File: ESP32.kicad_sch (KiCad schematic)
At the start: 1 part

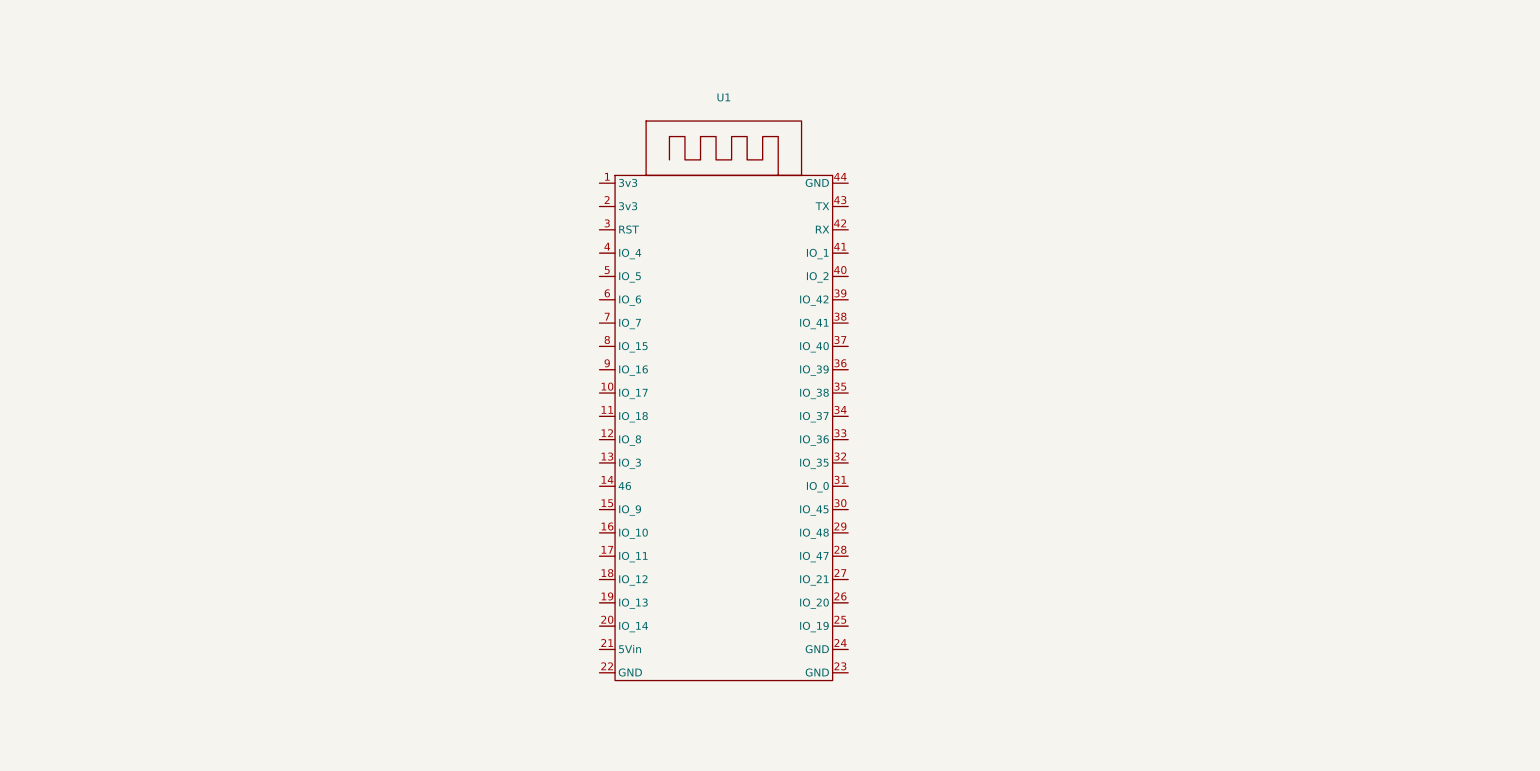
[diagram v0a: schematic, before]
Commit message: added all block interface pins
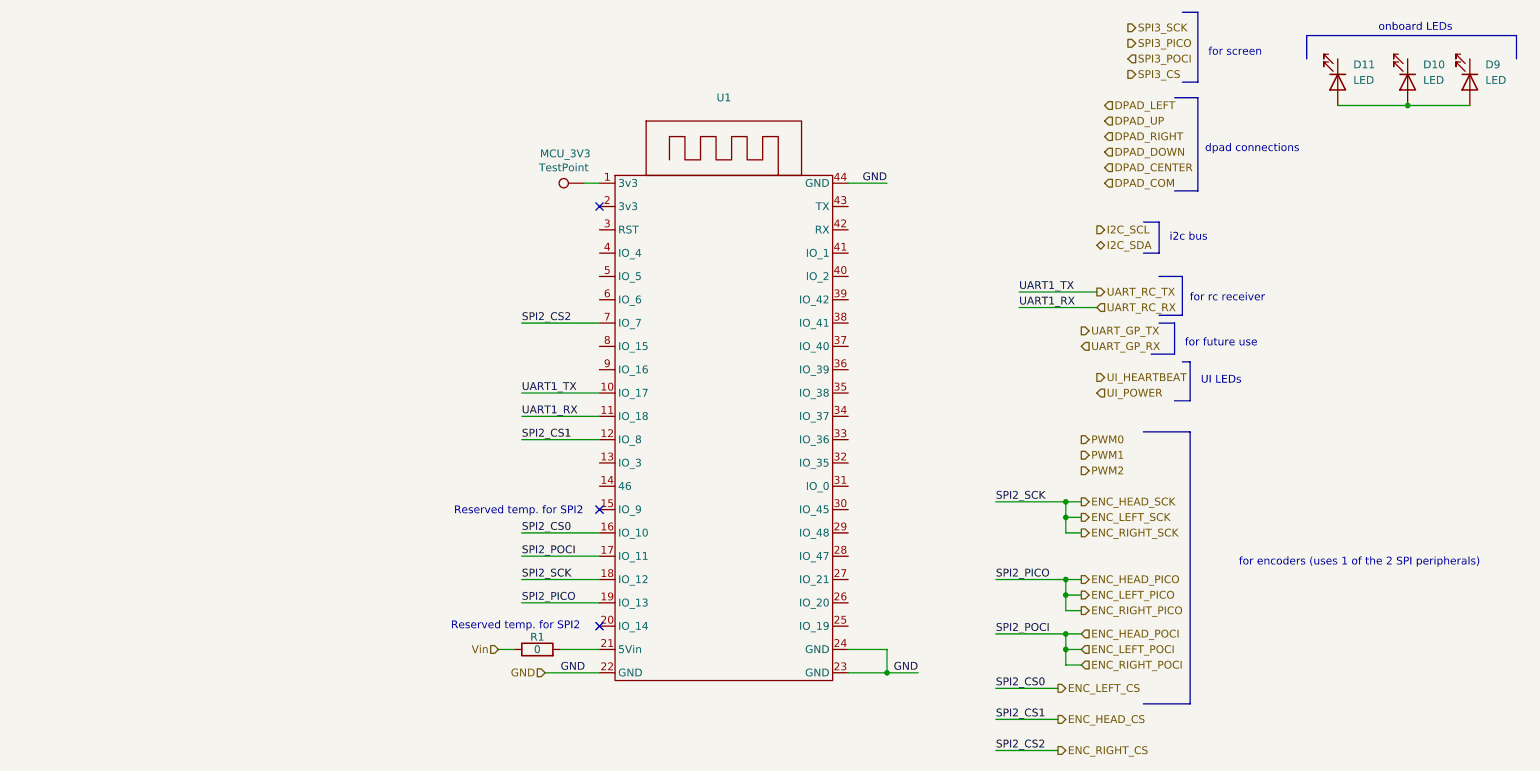
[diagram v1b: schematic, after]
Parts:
- added D10, D11, D9: LED, symbol Device:LED
- added MCU_3V3: TestPoint, symbol Connector:TestPoint
- added R1: 0, symbol Device:R
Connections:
- net at U1.1 (3v3): now also MCU_3V3.1
- net UART_RC_TX: now reaches U1.10 (IO_17)
- net UART_RC_RX: now reaches U1.11 (IO_18)
- net ENC_HEAD_CS: now reaches U1.12 (IO_8)
- net ENC_LEFT_CS: now reaches U1.16 (IO_10)
- net ENC_HEAD_POCI: now reaches U1.17 (IO_11)
- net ENC_HEAD_SCK: now reaches U1.18 (IO_12)
- net ENC_HEAD_PICO: now reaches U1.19 (IO_13)
- net at U1.21 (5Vin): now also R1.2
- net GND: now reaches U1.22 (GND)
- net GND: now also U1.23 (GND), U1.24 (GND), U1.44 (GND)
- net ENC_RIGHT_CS: now reaches U1.7 (IO_7)
- new net: D10.2 (A), D11.2 (A), D9.2 (A)
- new net Vin: R1.1
- no-connect marks 0 -> 3
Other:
- note added: "Reserved temp. for SPI2"
- note added: "UI LEDs"
- note added: "dpad connections"
- note added: "for encoders (uses 1 of the 2 SPI peripherals)"
- note added: "for future use"
- note added: "for rc receiver"
- note added: "for screen"
- note added: "i2c bus"
- note added: "onboard LEDs"

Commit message: ESP32 mostly done
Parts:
- removed D10, D11, D9: LED, symbol Device:LED
- added Q1, Q2: BSS138, Package_TO_SOT_SMD:SOT-23, symbol Transistor_FET:BSS138
- added R2, R3, R4, R5, R6, R7: R, symbol Device:R
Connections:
- net GND is gone; now on net DPAD_COM: U1.22 (GND), U1.23 (GND), U1.24 (GND), U1.44 (GND)
- net DPAD_CENTER: now also U1.4 (IO_4)
- net DPAD_DOWN: now also U1.13 (IO_3)
- net DPAD_LEFT: now also U1.31 (IO_0)
- net DPAD_RIGHT: now also U1.41 (IO_1)
- net DPAD_UP: now also U1.40 (IO_2)
- net ENC_HEAD_CS: now also U1.5 (IO_5); no longer U1.12 (IO_8)
- net ENC_LEFT_CS: now also U1.6 (IO_6); no longer U1.16 (IO_10)
- net I2C_SCL: now also U1.9 (IO_16), R2.2
- net I2C_SDA: now also U1.8 (IO_15), R3.2
- net UART_GP_RX: now also U1.28 (IO_47)
- net UART_GP_TX: now also U1.29 (IO_48)
- net UART_RC_RX: no longer U1.11 (IO_18)
- net UART_RC_TX: no longer U1.10 (IO_17)
- net UI_HEARTBEAT: now also U1.38 (IO_41)
- net UI_POWER: now also U1.37 (IO_40)
- net PWM_HEAD: now reaches U1.25 (IO_19)
- net PWM_LEFT: now reaches U1.26 (IO_20)
- net PWM_RIGHT: now reaches U1.27 (IO_21)
- net SCREEN_CS: now reaches U1.33 (IO_36)
- net SCREEN_POCI: now reaches U1.34 (IO_37)
- net SCREEN_PICO: now reaches U1.35 (IO_38)
- net SCREEN_SCK: now reaches U1.36 (IO_39)
- new net: Q2.3 (D), R7.2
- new net: Q2.1 (G), R6.2
- new net: Q2.2 (S), R6.1
- new net: Q1.1 (G), R4.1
- new net: Q1.2 (S), R4.2
- new net: Q1.3 (D), R5.2
- new net 3V3_IN: R2.1, R3.1
- new net UART1_RX: U1.11 (IO_18)
- new net UART1_TX: U1.10 (IO_17)
- no-connect marks 3 -> 1
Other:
- note added: "ADD INVERTER & logic level converter for rc"
- note removed: "Reserved temp. for SPI2"
- note removed: "UI LEDs"
- note removed: "dpad connections"
- note removed: "for encoders (uses 1 of the 2 SPI peripherals)"
- note removed: "for future use"
- note removed: "for rc receiver"
- note removed: "for screen"
- note removed: "i2c bus"
- note removed: "onboard LEDs"
